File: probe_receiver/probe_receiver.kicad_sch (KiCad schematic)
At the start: 9 parts, among them J1 Conn_01x05_Female, K1 HE721C0510, Q1 2N2907A, U1 TSSP4038

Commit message: - add fix for PCB v1.1 (fix resistor place 1608)
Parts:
- R1, R2, R3: footprint Resistor_SMD:R_0201_0603Metric -> Resistor_SMD:R_0603_1608Metric
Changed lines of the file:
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@@
       (effects (font (size 1.27 1.27)) (justify left))
     )
-    (property "Footprint" "Resistor_SMD:R_0201_0603Metric" (id 2) (at 191.262 76.2 90)
+    (property "Footprint" "Resistor_SMD:R_0603_1608Metric" (id 2) (at 191.262 76.2 90)
       (effects (font (size 1.27 1.27)) hide)
     )
@@
       (effects (font (size 1.27 1.27)) (justify left))
     )
-    (property "Footprint" "Resistor_SMD:R_0201_0603Metric" (id 2) (at 188.722 44.45 90)
+    (property "Footprint" "Resistor_SMD:R_0603_1608Metric" (id 2) (at 188.722 44.45 90)
       (effects (font (size 1.27 1.27)) hide)
     )
@@
     (property "Reference" "R1" (id 0) (at 161.29 45.72 90))
     (property "Value" "R39" (id 1) (at 161.29 48.26 90))
-    (property "Footprint" "Resistor_SMD:R_0201_0603Metric" (id 2) (at 161.29 53.848 90)
+    (property "Footprint" "Resistor_SMD:R_0603_1608Metric" (id 2) (at 161.29 53.848 90)
       (effects (font (size 1.27 1.27)) hide)
     )
@@
     )
     (path "/2a8476bf-0961-4956-a574-8948f6fba40c"
-      (reference "R1") (unit 1) (value "R39") (footprint "Resistor_SMD:R_0201_0603Metric")
+      (reference "R1") (unit 1) (value "R39") (footprint "Resistor_SMD:R_0603_1608Metric")
     )
     (path "/0ee65aa9-7553-4e36-9c0f-37531b66b588"
-      (reference "R2") (unit 1) (value "R1K") (footprint "Resistor_SMD:R_0201_0603Metric")
+      (reference "R2") (unit 1) (value "R1K") (footprint "Resistor_SMD:R_0603_1608Metric")
     )
     (path "/05a92e07-fb02-487b-9422-f9dcd938e639"
-      (reference "R3") (unit 1) (value "R1K") (footprint "Resistor_SMD:R_0201_0603Metric")
+      (reference "R3") (unit 1) (value "R1K") (footprint "Resistor_SMD:R_0603_1608Metric")
     )
     (path "/3a754a86-fa7b-4cf0-aebc-1a1b1711d1e1"

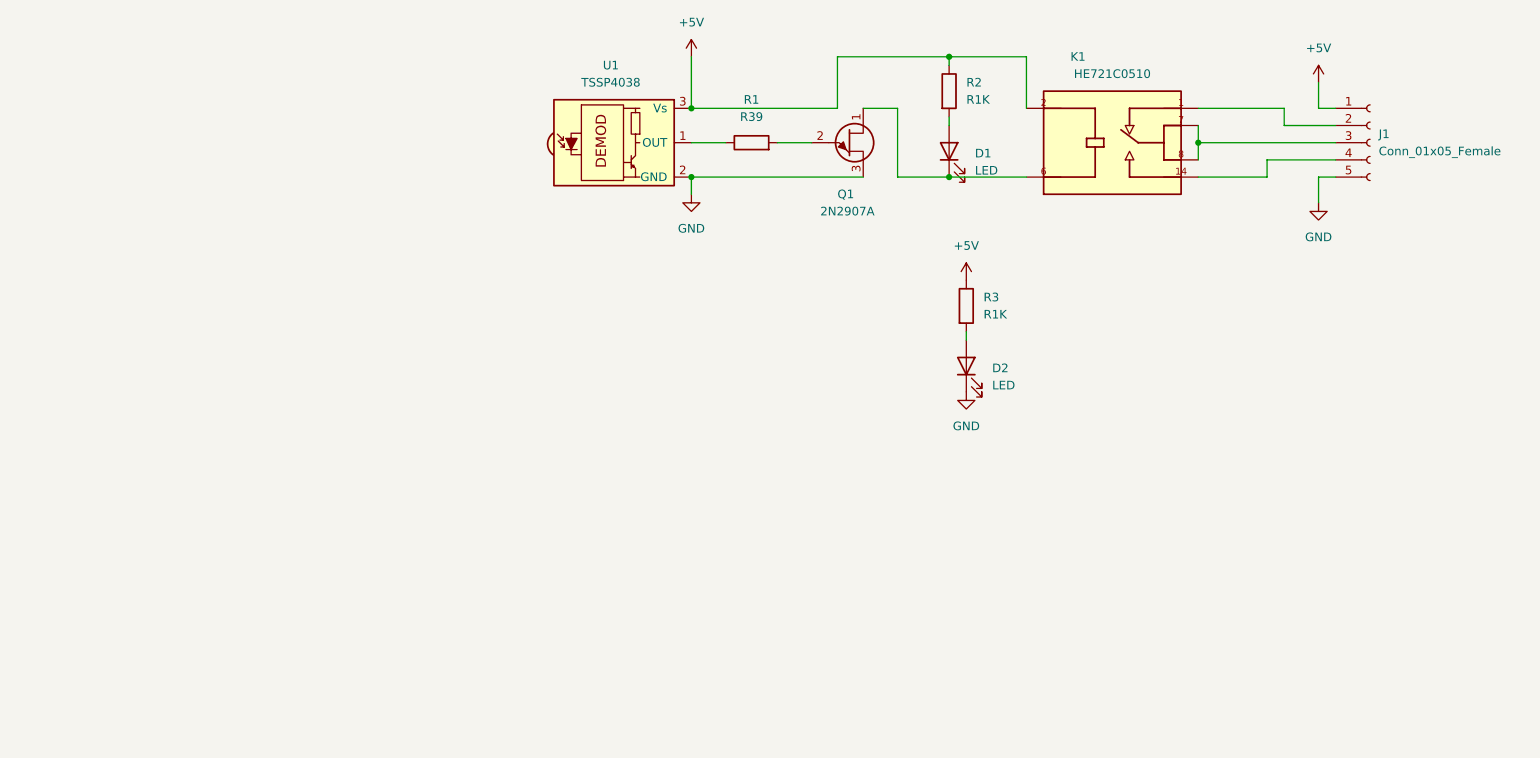
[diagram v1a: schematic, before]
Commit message: - update probe reciver to v1.1
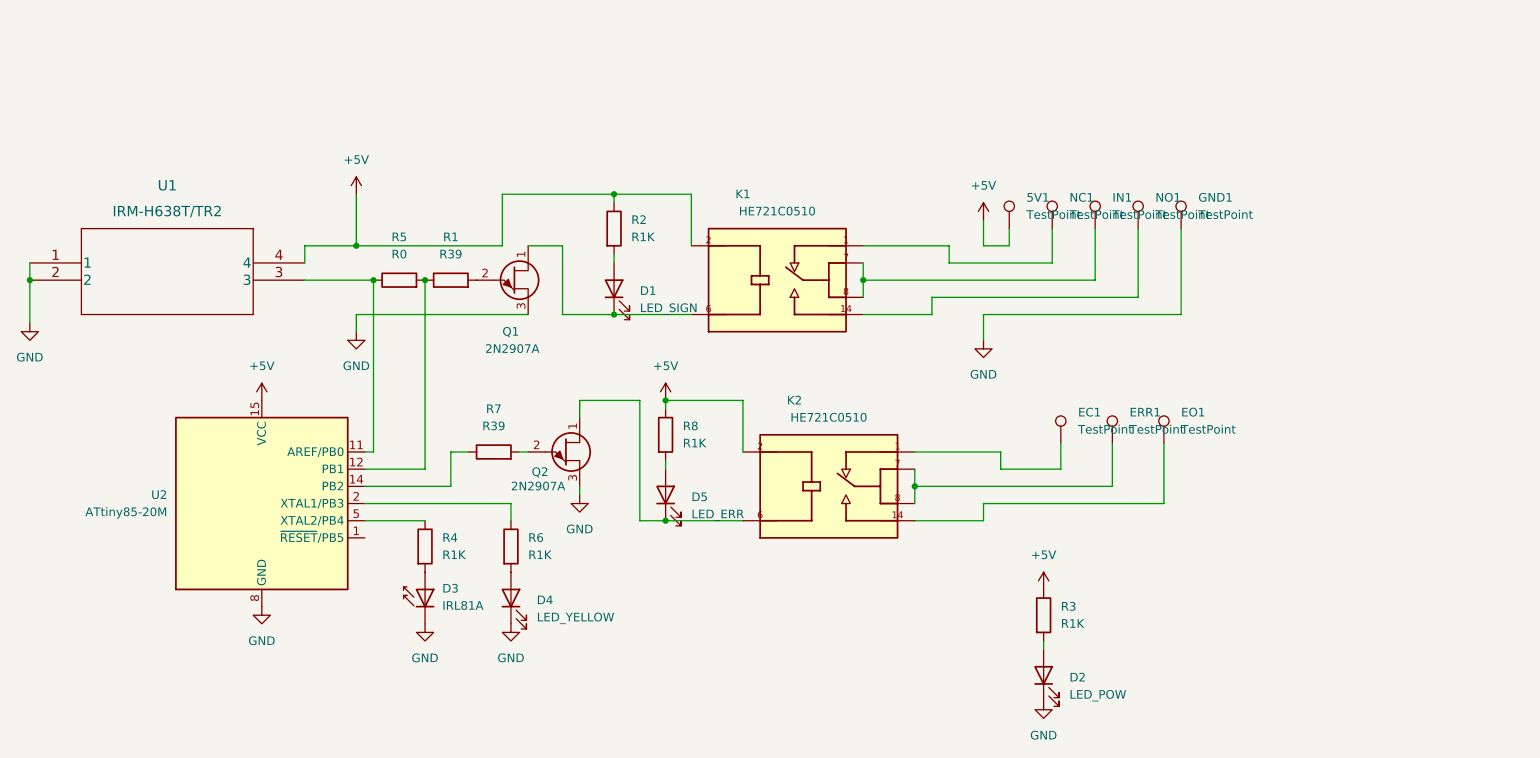
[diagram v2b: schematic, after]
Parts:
- removed J1: Conn_01x05_Female, Connector_PinSocket_2.54mm:PinSocket_1x05_P2.54mm_Vertical, symbol Connector:Conn_01x05_Female
- removed U1: TSSP4038, OptoDevice:Vishay_MINICAST-3Pin, symbol Sensor_Proximity:TSSP58P38
- added 5V1: TestPoint, symbol Connector:TestPoint
- added D3: IRL81A, LED_THT:LED_SideEmitter_Rectangular_W4.5mm_H1.6mm, symbol LED:IRL81A
- added D4: LED_YELLOW, LED_SMD:LED_0805_2012Metric, symbol Device:LED
- added D5: LED_ERR, LED_SMD:LED_0805_2012Metric, symbol Device:LED
- added EC1, EO1, ERR1, GND1, IN1, NC1, NO1: TestPoint, TestPoint:TestPoint_Pad_D2.0mm, symbol Connector:TestPoint
- added K2: HE721C0510, RELAY_HE721C0510, symbol HE721C0510:HE721C0510
- added Q2: 2N2907A, Package_TO_SOT_THT:TO-18-3, symbol Transistor_BJT:2N2646
- added R4, R6, R8: R1K, Resistor_SMD:R_0603_1608Metric, symbol Device:R
- added R5: R0, Resistor_SMD:R_0201_0603Metric, symbol Device:R
- added R7: R39, Resistor_SMD:R_0603_1608Metric, symbol Device:R
- added U1: IRM-H638T/TR2, IRM-H638T-TR2:IRM-H638T&slash_TR2_EVE, symbol IRM-H638T-TR2:IRM-H638T/TR2
- added U2: ATtiny85-20M, Package_DFN_QFN:QFN-20-1EP_4x4mm_P0.5mm_EP2.6x2.6mm, symbol MCU_Microchip_ATtiny:ATtiny85-20M
- D1: value LED -> LED_SIGN
- D2: value LED -> LED_POW
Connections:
- net +5V: now also 5V1.1, K2.2, R8.1, U1.4, U2.15 (VCC)
- net GND: now also D3.1 (K), D4.1 (K), GND1.1, Q2.3 (B1), U1.1, U1.2, U2.21 (GND), U2.8 (GND)
- net at R1.1: now also R5.2, U2.12 (PB1)
- net at K1.1: now also NC1.1
- net at K1.14: now also NO1.1
- net at K1.7, K1.8: now also IN1.1
- new net: D4.2 (A), R6.2
- new net: EO1.1, K2.14
- new net: D5.2 (A), R8.2
- new net: D5.1 (K), K2.6, Q2.1 (B2)
- new net: R5.1, U1.3, U2.11 (AREF/PB0)
- new net: ERR1.1, K2.7, K2.8
- new net: Q2.2 (E), R7.2
- new net: R4.1, U2.5 (XTAL2/PB4)
- new net: D3.2 (A), R4.2
- new net: EC1.1, K2.1
- new net: R7.1, U2.14 (PB2)
- new net: R6.1, U2.2 (XTAL1/PB3)
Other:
- moved on the sheet: D1, D2, K1, Q1, R1, R2, R3

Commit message: -update version Kicad
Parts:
- 5V1: footprint (none) -> TestPoint:TestPoint_Pad_D2.0mm
- U1: symbol IRM-H638T-TR2:IRM-H638T/TR2 -> IRM-H638T-TR2:IRM-H638T/TR2
